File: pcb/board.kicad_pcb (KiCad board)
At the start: 2 copper layers, 159.9 x 99.9 mm, 170 parts, among them J1 Conn_02x03_Counter_Clockwise, J2 USB_B, J3 650913-5, SW1 SW_Push, U1 XC6SLX16-FTG256, U10 TPS541620, U11 74LVC1G08, U12 IS42S16100H, U13 IS42S16100H, U14 ECS-7050MV, U15 BCM56DS, U16 74LVC1G32, U17 74LS04, U18 74LS08, U19 LMC555xMM, U2 74LVC157, U3 AT25xxx, U4 TMUX1219, U5 AT25xxx, U6 74LVC1G04, U7 SN74AVC4T245PW, U8 FT2232HQ, U9 93LCxxBxxOT, Y1 12MHz

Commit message: start placing components
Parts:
- C34: footprint Capacitor_SMD:CP_Elec_4x4.5 -> Capacitor_SMD:C_1210_3225Metric
- moved C40 231.2 mm to (79.3, 194.9), turned to 180 degrees
- moved U7 225.8 mm to (120.1, 206.9)
- moved C39 225.2 mm to (75.8, 189.7), turned to -90 degrees
- moved C42 219.8 mm to (85.9, 194.9)
- moved U8 218.1 mm to (82.1, 188.9)
- moved C29 214.9 mm to (128.9, 188.9)
- moved C30 214.9 mm to (120.2, 198.8)
- moved C35 214.9 mm to (117.3, 198.7)
- moved C36 214.9 mm to (116.5, 184.4)
- moved C37 214.9 mm to (136.6, 182.5)
- moved C44 214.9 mm to (126.0, 190.3)
- moved C45 214.9 mm to (136.5, 184.5)
- moved C46 214.9 mm to (128.9, 187.0)
- moved C47 214.9 mm to (120.2, 196.8)
- moved C48 214.9 mm to (133.7, 184.5)
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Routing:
- added copper zone on B.Cu, net GND
- added copper zone on F.Cu, net GND
- added copper zone on In1.Cu, net GND
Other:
- copper layers 2 -> 4

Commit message: place components relative to each others
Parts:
- removed C47: 0.1u, Capacitor_SMD:C_0402_1005Metric
- moved C35 241.2 mm to (111.2, -42.5)
- moved C94 231.3 mm to (78.9, 70.2)
- moved U15 229.0 mm to (68.1, 63.4), turned to 180 degrees
- moved R37 228.0 mm to (67.1, 66.9)
- moved C92 225.2 mm to (70.5, 69.7)
- moved C91 219.9 mm to (72.1, 54.7), turned to 180 degrees
- moved R12 219.6 mm to (112.2, -46.5)
- moved R39 216.8 mm to (81.9, 64.8), turned to 90 degrees
- moved U18 215.6 mm to (74.6, 60.2), turned to 90 degrees
- moved R36 214.9 mm to (67.1, 68.9)
- moved C96 210.6 mm to (75.2, 70.2)
- moved U16 207.6 mm to (71.0, 67.2), turned to 180 degrees
- moved C93 201.7 mm to (86.0, 61.7), turned to 90 degrees
- moved R38 201.1 mm to (79.7, 64.3)
- moved U17 201.0 mm to (82.1, 59.3), turned to -90 degrees
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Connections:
- C34 pad 1: Net-(C34-Pad1) -> VCCAUX
- C71 pad 2: VCCAUX -> GND
- C91 pad 2: VCCAUX -> GND
- C92 pad 2: VCCAUX -> GND
- C93 pad 2: VCCAUX -> GND
- C94 pad 1: VCCAUX -> GND
- C95 pad 2: VCCAUX -> GND
- C96 pad 2: VCCAUX -> GND
- D3 pad 2: VCCAUX -> GND
- SW1 pad 2: VCCAUX -> GND
- U1 pad P14: VCCAUX -> GND
- U11 pad 5: VCCAUX -> GND
- U16 pad 3: VCCAUX -> GND
- U17 pad 7: VCCAUX -> GND
- U18 pad 7: VCCAUX -> GND
- U19 pad 1: VCCAUX -> GND
- U8 pad 12: Net-(C34-Pad1) -> VCCAUX
- U8 pad 37: Net-(C34-Pad1) -> VCCAUX
- U8 pad 49: Net-(C34-Pad1) -> VCCAUX
- U8 pad 64: Net-(C34-Pad1) -> VCCAUX

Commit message: keep working on the pcb
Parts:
- removed C64, C68: open, Capacitor_SMD:C_0603_1608Metric
- added C47: 100uF, Capacitor_SMD:C_1210_3225Metric, F.Cu at (226.1, 13.7)
- C55, C56, C63: footprint Capacitor_SMD:C_0603_1608Metric -> Capacitor_SMD:C_0402_1005Metric
- moved C69 53.7 mm to (226.1, 21.2), turned to 180 degrees
- moved L2 53.3 mm to (225.6, 26.8), turned to 0 degrees
- moved L1 51.4 mm to (216.6, 26.8), turned to 180 degrees
- moved C70 49.2 mm to (226.1, 17.5), turned to 180 degrees
- moved C53 47.0 mm to (213.3, 33.4), turned to -90 degrees
- moved C60 45.7 mm to (232.1, 33.4), turned to -90 degrees
- moved C54 45.0 mm to (215.6, 33.4), turned to -90 degrees
- moved C61 43.0 mm to (228.8, 33.4), turned to -90 degrees
- moved U10 42.2 mm to (221.1, 34.2), turned to -90 degrees
- moved C56 40.0 mm to (219.6, 31.4)
- moved C62 39.9 mm to (226.6, 33.4), turned to -90 degrees
- moved C57 38.0 mm to (216.1, 21.2)
- moved C51 36.8 mm to (198.4, 52.9), turned to 90 degrees
- moved C63 34.8 mm to (224.8, 33.4), turned to -90 degrees
- moved C58 32.4 mm to (216.1, 17.4)
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
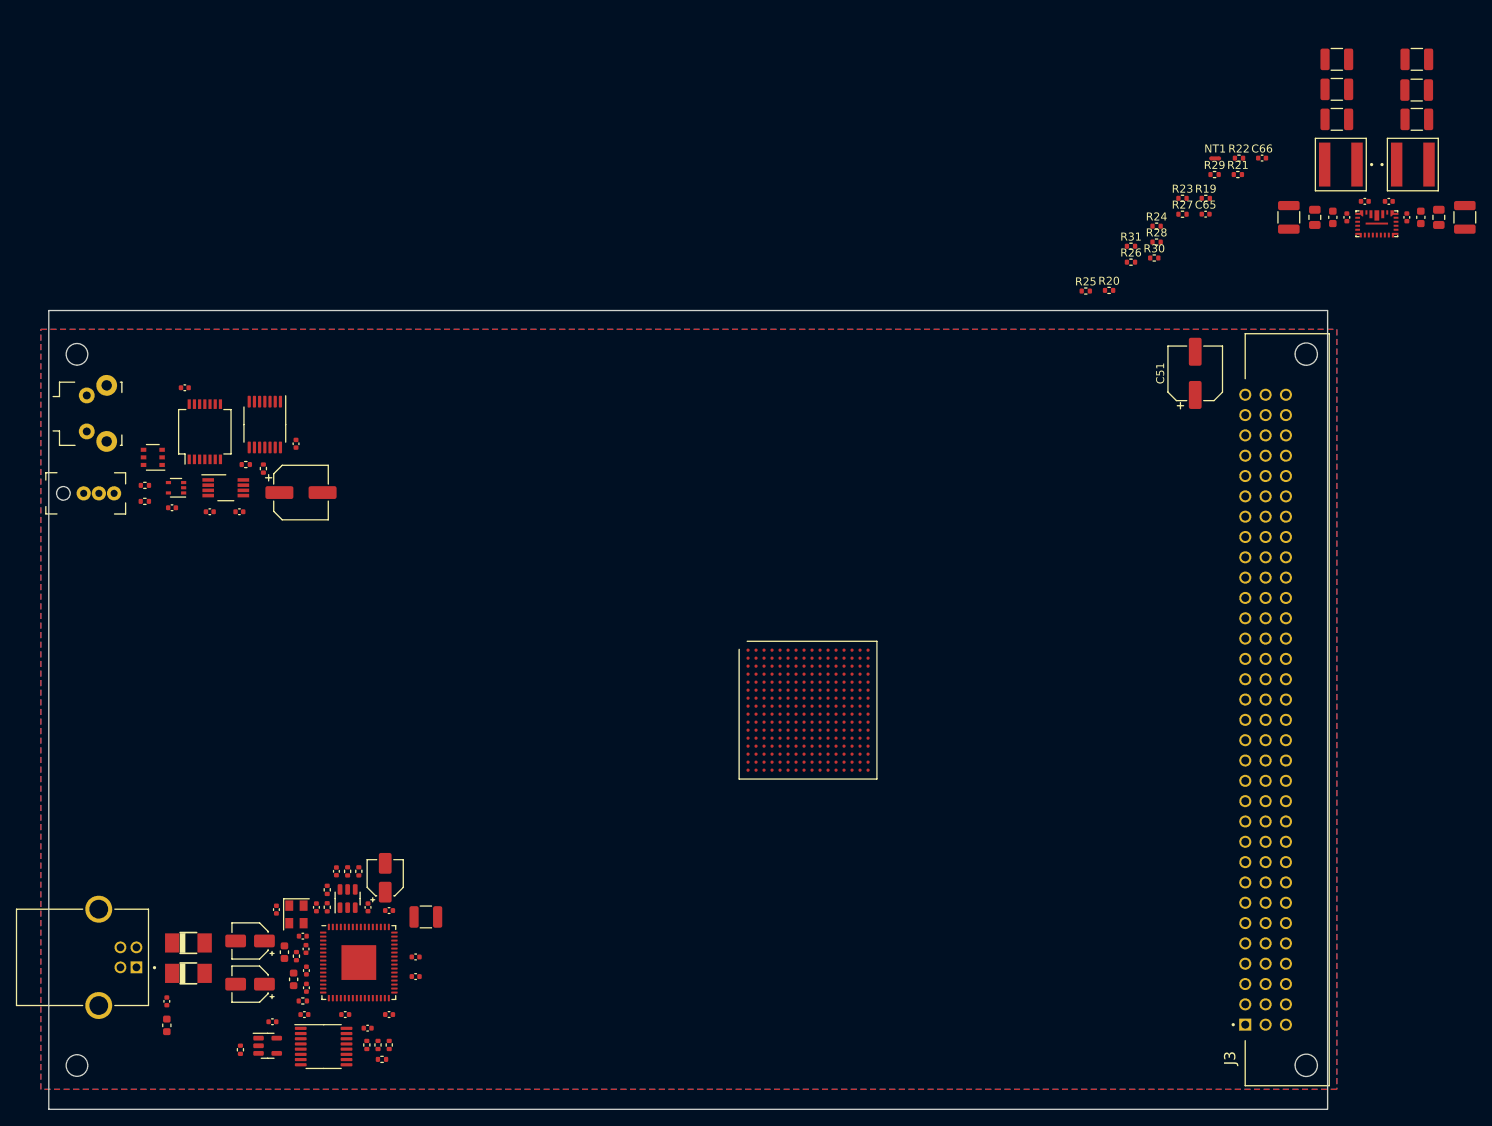
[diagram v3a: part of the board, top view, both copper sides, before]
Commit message: add traces for the power supply
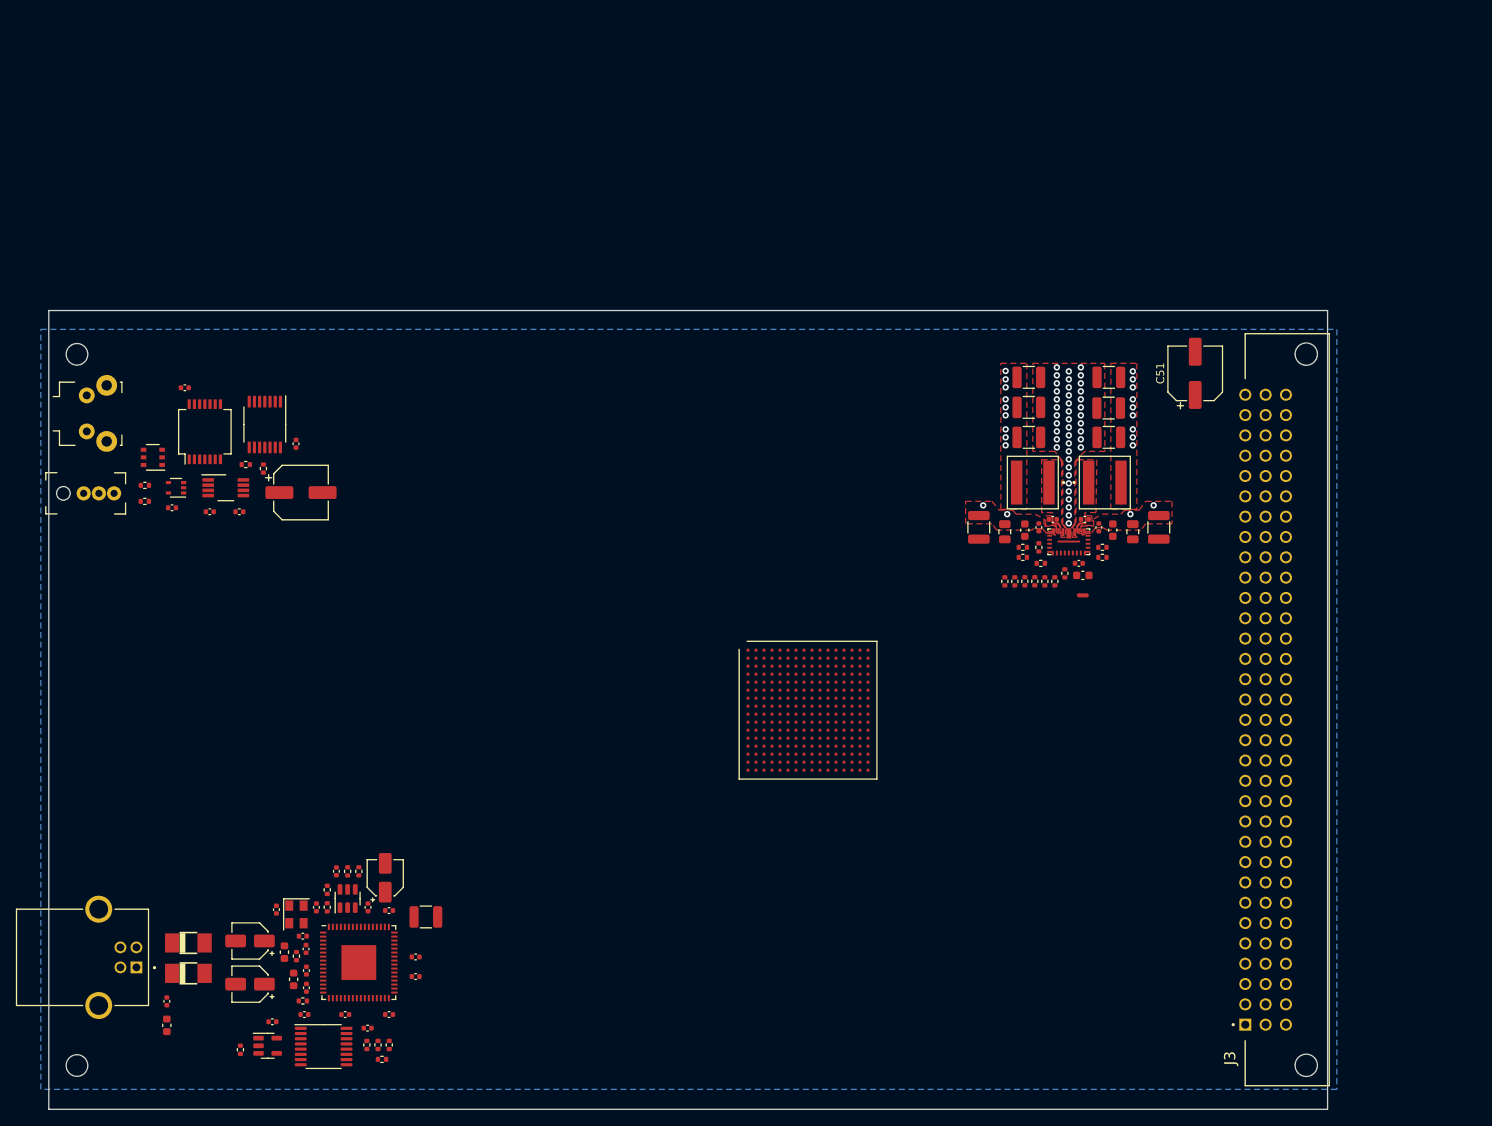
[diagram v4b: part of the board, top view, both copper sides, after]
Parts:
- C65: footprint Capacitor_SMD:C_0402_1005Metric -> Capacitor_SMD:C_0603_1608Metric
- moved R22 59.3 mm to (177.1, 78.9), turned to 90 degrees
- moved NT1 57.1 mm to (184.3, 80.7), turned to 180 degrees
- moved R29 56.7 mm to (175.8, 78.9), turned to -90 degrees
- moved R21 56.3 mm to (179.6, 78.9), turned to 90 degrees
- moved C56 55.7 mm to (180.6, 71.2)
- moved C66 55.6 mm to (183.8, 76.7)
- moved U10 55.3 mm to (182.6, 74.0)
- moved C47 55.3 mm to (187.6, 53.4)
- moved C57 55.3 mm to (177.6, 60.9)
- moved C58 55.3 mm to (177.6, 57.2)
- moved C59 55.3 mm to (177.6, 53.4)
- moved C69 55.3 mm to (187.6, 60.9)
- moved C70 55.3 mm to (187.6, 57.3)
- moved L1 55.3 mm to (178.1, 66.6)
- moved L2 55.3 mm to (187.1, 66.6)
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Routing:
- net VCCINT: vias 0 -> 9
- net VCCAUX: vias 0 -> 9
- net VCC: vias 0 -> 4
- net GND: vias 0 -> 42
- added copper zone on F.Cu, net Net-(C56-Pad1)
- added copper zone on F.Cu, net Net-(C56-Pad2)
- added copper zone on F.Cu, net Net-(C67-Pad1)
- added copper zone on F.Cu, net Net-(C67-Pad2)
- added copper zone on F.Cu, net VCC
- added copper zone on F.Cu, net VCCAUX
- added copper zone on F.Cu, net VCCINT

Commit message: change to lx9 and reduce power
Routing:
- net GND: vias 42 -> 47
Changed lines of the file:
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@@
   (via (at 182.58 54.68) (size 0.8) (drill 0.4) (layers "F.Cu" "B.Cu") (free) (net 2))
   (via (at 182.58 71.68) (size 0.8) (drill 0.4) (layers "F.Cu" "B.Cu") (free) (net 2))
+  (via (at 183.93 73.98) (size 0.6) (drill 0.3) (layers "F.Cu" "B.Cu") (net 2))
+  (via locked (at 183.03 73.98) (size 0.6) (drill 0.3) (layers "F.Cu" "B.Cu") (net 2))
   (via (at 181.08 59.18) (size 0.8) (drill 0.4) (layers "F.Cu" "B.Cu") (free) (net 2))
   (via (at 182.58 68.68) (size 0.8) (drill 0.4) (layers "F.Cu" "B.Cu") (free) (net 2))
@@
   (via (at 182.58 66.68) (size 0.8) (drill 0.4) (layers "F.Cu" "B.Cu") (free) (net 2))
   (via (at 184.08 60.18) (size 0.8) (drill 0.4) (layers "F.Cu" "B.Cu") (free) (net 2))
+  (via (at 182.13 73.98) (size 0.6) (drill 0.3) (layers "F.Cu" "B.Cu") (net 2))
   (via (at 182.58 69.68) (size 0.8) (drill 0.4) (layers "F.Cu" "B.Cu") (free) (net 2))
   (via (at 184.08 59.18) (size 0.8) (drill 0.4) (layers "F.Cu" "B.Cu") (free) (net 2))
@@
   (via (at 182.58 52.68) (size 0.8) (drill 0.4) (layers "F.Cu" "B.Cu") (free) (net 2))
   (via (at 184.08 54.18) (size 0.8) (drill 0.4) (layers "F.Cu" "B.Cu") (free) (net 2))
+  (via (at 181.23 73.98) (size 0.6) (drill 0.3) (layers "F.Cu" "B.Cu") (net 2))
   (via (at 181.08 53.18) (size 0.8) (drill 0.4) (layers "F.Cu" "B.Cu") (free) (net 2))
   (via (at 184.08 52.18) (size 0.8) (drill 0.4) (layers "F.Cu" "B.Cu") (free) (net 2))
   (via (at 182.58 70.68) (size 0.8) (drill 0.4) (layers "F.Cu" "B.Cu") (free) (net 2))
+  (via (at 183.93 73.98) (size 0.6) (drill 0.3) (layers "F.Cu" "B.Cu") (net 2))
   (via (at 184.08 57.18) (size 0.8) (drill 0.4) (layers "F.Cu" "B.Cu") (free) (net 2))
   (via (at 182.58 63.68) (size 0.8) (drill 0.4) (layers "F.Cu" "B.Cu") (free) (net 2))
@@
       )
     )
+  )
+  (zone (net 2) (net_name "GND") (layer "F.Cu") (hatch edge 0.508)
+    (connect_pads yes (clearance 0.14))
+    (min_thickness 0.127) (filled_areas_thickness no)
+    (fill yes (thermal_gap 0.508) (thermal_bridge_width 0.508))
+    (polygon
+      (pts
+        (xy 179.68 73.03)
+        (xy 180.48 73.03)
+        (xy 180.68 73.23)
+        (xy 180.98 73.23)
+        (xy 181.18 73.03)
+        (xy 181.38 73.03)
+        (xy 181.48 73.13)
+        (xy 181.48 73.43)
+        (xy 181.58 73.53)
+        (xy 183.58 73.53)
+        (xy 183.68 73.43)
+        (xy 183.68 73.13)
+        (xy 183.78 73.03)
+        (xy 183.98 73.03)
+        (xy 184.18 73.23)
+        (xy 184.48 73.23)
+        (xy 184.68 73.03)
+        (xy 185.48 73.03)
+        (xy 185.98 72.33)
+        (xy 186.58 72.33)
+        (xy 187.18 72.63)
+        (xy 195.58 72.63)
+        (xy 195.58 74.63)
+        (xy 189.58 74.63)
+        (xy 189.08 74.13)
+        (xy 186.78 74.13)
+        (xy 185.48 73.43)
+        (xy 184.68 73.43)
+        (xy 184.48 73.63)
+        (xy 184.48 74.93)
+        (xy 180.68 74.93)
+        (xy 180.68 73.63)
+        (xy 180.48 73.43)
+        (xy 178.38 73.43)
+        (xy 177.78 74.03)
+        (xy 175.98 74.03)
+        (xy 175.58 74.63)
+        (xy 169.58 74.63)
+        (xy 169.58 72.63)
+        (xy 177.98 72.63)
+        (xy 178.58 72.33)
+        (xy 179.08 72.33)
+      )
+    )
